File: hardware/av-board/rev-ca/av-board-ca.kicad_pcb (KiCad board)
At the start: 4 copper layers, 130 x 100 mm, 284 parts, among them J1 RCA Y, J11 XIAO 5V..D7, J12 XIAO D0..D6, J13 OPTICAL, J14 RCA S/PDIF, J15 USB-C 5V, J16 JTAG, J2 RCA Pb, J20 DF40HC(3.0)-80DS, J21 DF40HC(3.0)-100DS, J22 DF40HC(3.0)-100DS, J3 RCA Pr, J4 RCA L, J5 RCA R, J6 HDMI-001, J7 SYNC, J8 VGA, Q1 2N7002, Q2 2N7002, Q3 2N7002, Q4 2N7002, SW1 TS-1187A-B-A-B, SW2 TS-1187A-B-A-B, SW3 TS-1187A-B-A-B, U1 ADV7181DBCPZ-RL, U10 TPD4E05U06DQAR, U12 TPS7A2045PDBVR, U13 SN74LVC1GU04DBVR, U14 SN74LVC1G04DBVR, U15 SN74LVC1G04DBVR, U17 MS5351M, U19 TPD4E05U06DQAR, U2 ADV7511KSTZ, U20 TPD4E05U06DQAR, U21 SN74LVC2G17DBVR, U22 SN74LVC8T245PWR, U23 SN74AVC4T245PWR, U24 ME6211C30M5G-N, U3 PCM1808PWR, U4 TLV62569DBVR, U5 TPS7A7001DDAR, U6 TPS7A7001DDAR, U7 TPS7A7001DDAR, U8 TPD4E05U06DQAR, U9 TPD4E05U06DQAR, Y1 28.63636MHz 20pF, Y2 25MHz 10pF

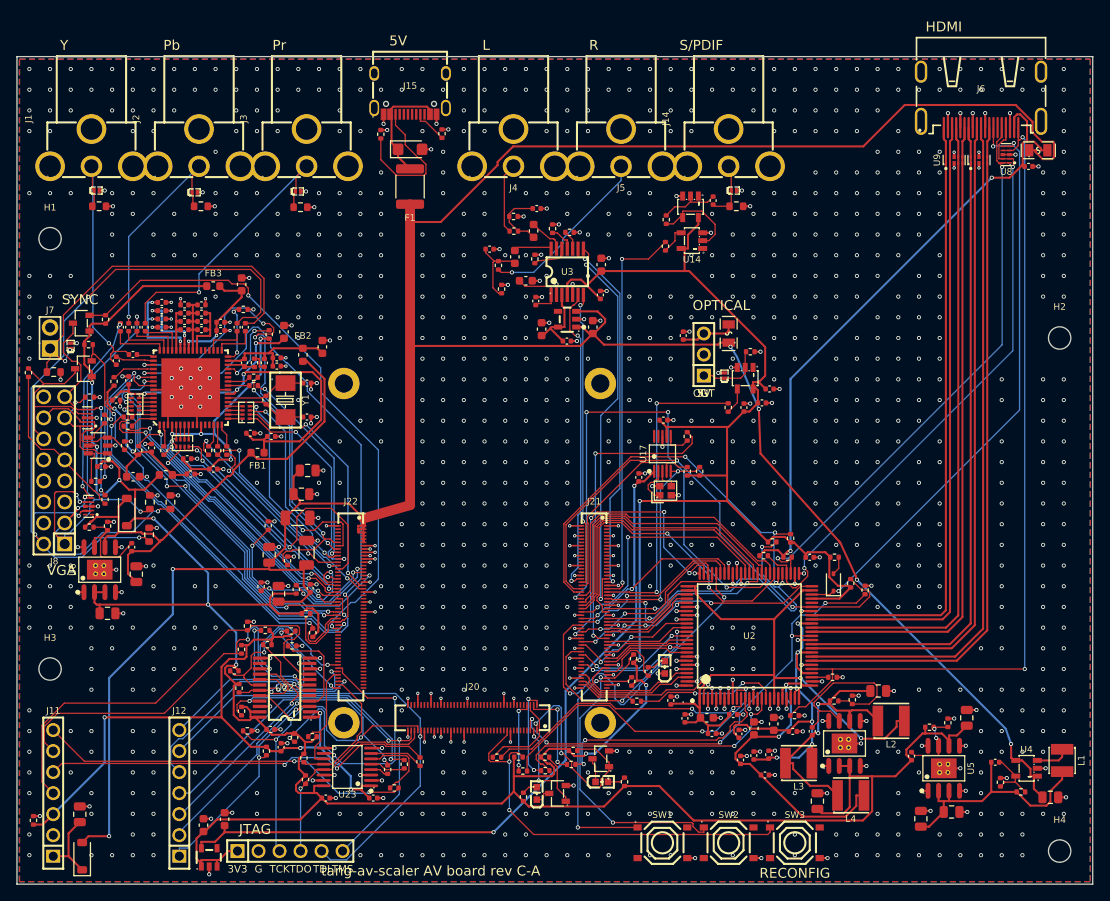
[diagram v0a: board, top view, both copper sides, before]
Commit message: AV boards: the last complete, valid design of each revision; decoupling at the pins
Each revision's board, schematic, fab files and renders are its last complete
route: DRC clean, no unconnected items, ERC clean, the board equal to its
schematic part for part (pads, values, footprints; only the mounting holes
H1-H4 have no symbol).

- Rev A: the silkscreen pass (labels clear of pads, texts and part bodies);
  copper unchanged.
- Rev B: the previous route with the silkscreen pass. Its schematic stays the
  one it was routed from: board.py now numbers eight capacitors the other way
  round, and its placement fixes (below) are not routed yet, the routes on the
  new placement having left 1 and 3 connections (review.md, Status).
- C-A: routed again on the fixed placement (try-ca-p1), the copper the router
  laid twice over taken up (218 segments).
- C-B: S/PDIF on rev B's 5-pin header instead of the coax jack, the HDMI
  receptacle next to the RCAs, the board 100 x 100 mm; routed again on the
  fixed placement (try-cb-p3). 5.4 mm of copper laid side by side in five
  nets is left (rev-c/review.md).

The review found decoupling not at the pins on every board (ADV7511 9-25 mm,
DP159 6-13 mm, the bucks' input capacitor by EN, the LDOs' capacitors, the
clock LDOs 73-80 mm from their chip) and C's VBUS_IN 0.25 mm wide for 2 A:
- parts.py: Part.at = "REF.PAD", the one pad a capacitor or filter serves;
  circuits, carrier.py and board.py name it for every regulator and supply pin
- pcbkit.py placer: ESD parts first, then small chips, then the at= capacitors
  and bias parts in board.py order; mean pin-to-capacitor distance on the
  placements: rev B 8.1 -> 3.6 mm, C-A 6.3 -> 3.3, C-B 5.5 -> 3.4
- rev C: VBUS_IN 0.7/1.2 mm into the TVS and fuse; rev B and C: the coax
  slicer placed first (SPDIF_AC a bias net); rev B: the buck U4 turned over

Kit: the silkscreen pass (labels clear of pads, texts, parts and the SOM,
reserved in the placer); prune takes up copper lying on another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
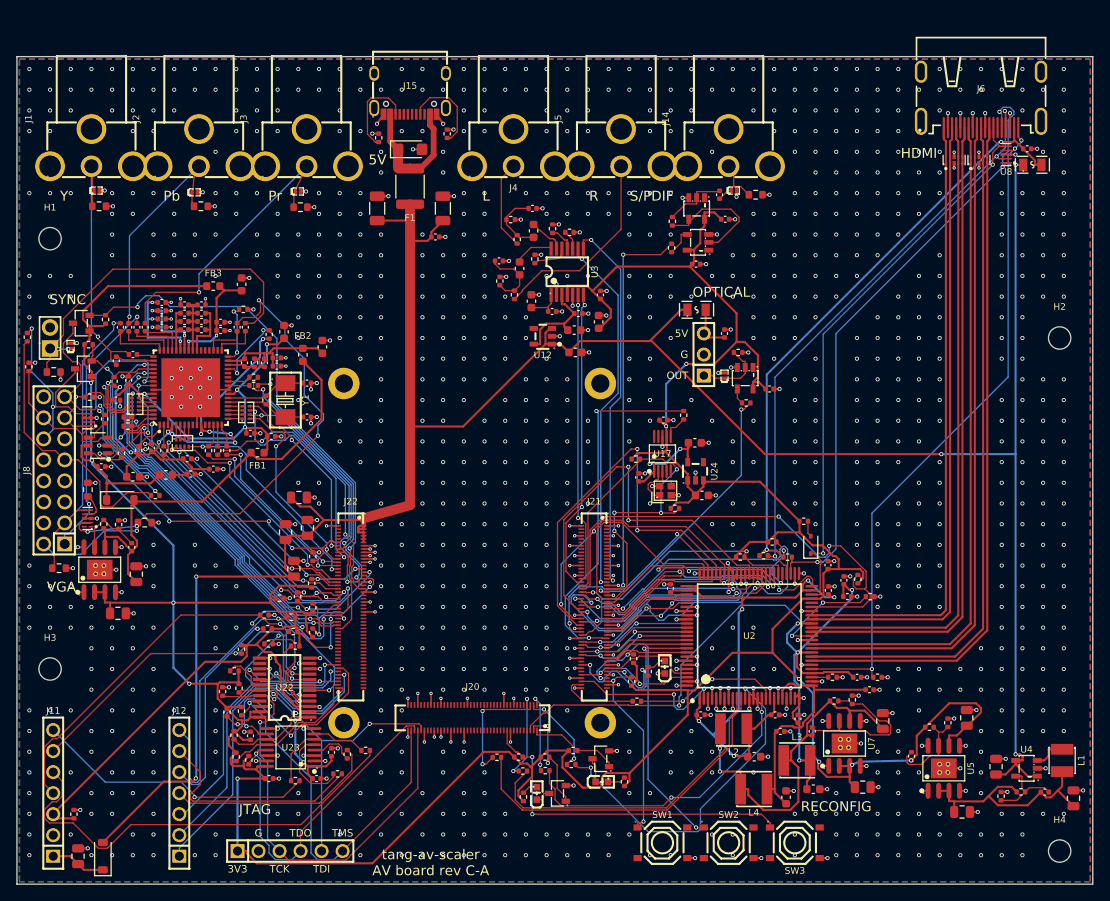
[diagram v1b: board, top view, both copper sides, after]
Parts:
- C11, C14, C8: value 10u -> 220p; footprint Capacitor_SMD:C_0805_2012Metric -> Capacitor_SMD:C_0402_1005Metric
- C12, C15, C9: value 220p -> 10u; footprint Capacitor_SMD:C_0402_1005Metric -> Capacitor_SMD:C_0805_2012Metric
- C5: value 10u -> 6.8p; footprint Capacitor_SMD:C_0805_2012Metric -> Capacitor_SMD:C_0402_1005Metric
- C6: value 6.8p -> 10u; footprint Capacitor_SMD:C_0402_1005Metric -> Capacitor_SMD:C_0805_2012Metric
- moved U24 75.0 mm to (182.0, 100.1)
- moved C80 72.8 mm to (181.9, 96.7), turned to 0 degrees
- moved C79 72.2 mm to (182.8, 103.0), turned to 0 degrees
- moved C3 45.1 mm to (150.6, 71.8), turned to 0 degrees
- moved C1 44.8 mm to (151.5, 68.3)
- moved C2 38.6 mm to (143.5, 68.3), turned to 90 degrees
- moved C93 23.8 mm to (199.9, 113.3)
- moved C70 21.2 mm to (185.6, 69.7)
- moved C92 21.1 mm to (200.3, 115.2), turned to 0 degrees
- moved L2 19.0 mm to (186.6, 131.2)
- moved C88 18.9 mm to (198.1, 114.5), turned to 90 degrees
- moved C71 18.6 mm to (182.1, 75.1)
- moved C89 18.3 mm to (179.0, 114.3), turned to 90 degrees
- moved C95 16.3 mm to (203.0, 126.5)
- moved R34 15.6 mm to (105.1, 111.8), turned to 0 degrees
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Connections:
- C11 pad 2: GND -> FB_1V8A
- C12 pad 2: FB_1V8A -> GND
- C14 pad 2: GND -> FB_1V8B
- C15 pad 2: FB_1V8B -> GND
- C5 pad 2: GND -> FB_3V6
- C6 pad 2: FB_3V6 -> GND
- C8 pad 2: GND -> FB_3V3
- C9 pad 2: FB_3V3 -> GND
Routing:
- net 3V0: track 89.6 -> 11.8 mm
- net +5V: track 344.9 -> 301.9 mm, vias 6 -> 5
- net OUT_R5: track 63.8 -> 28.0 mm, vias 4 -> 2
- net OUT_SDA: track 51.8 -> 29.0 mm, vias 3 -> 2
- net OUT_R3: track 21.1 -> 42.9 mm
- net IN_SDA: track 69.8 -> 48.2 mm
- net HDMI_HPD: track 103.2 -> 83.0 mm, vias 2 -> 3
- net XIAO_D6: track 25.3 -> 45.3 mm
- net JTAG_TDO: track 25.5 -> 42.4 mm
- net XIAO_D0: track 27.0 -> 43.7 mm, vias 2 -> 1
- net VGA_G: track 90.6 -> 75.1 mm, vias 4 -> 5
- net VGA_R: track 52.1 -> 37.4 mm, vias 4 -> 2
- net OUT_R7: track 39.1 -> 24.7 mm
- net FPGA_READY: track 25.2 -> 11.1 mm, vias 2 -> 0
- net TX_I2S0: track 27.5 -> 41.5 mm
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
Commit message: AV boards: silkscreen to JLCPCB's limits; the XIAO's way in printed on rev C
JLCPCB's silkscreen limits (its capabilities page): lines and strokes 0.15 mm
at least, text 1 mm high with a 1:6 stroke, 0.15 mm from pads.

- kit/pcbkit.py: designators and pin labels 1 mm (were 0.8 and 0.9 mm), every
  text's stroke 1:6 of its height; designators clear of the other parts'
  bodies, tried at 40 places beside their part before its own body.
  silk_tidy(): the parts' own silkscreen widened to 0.15 mm and cut back where
  it came within 0.15 mm of a pad, past the board's edge, under a text or onto
  another part's (the bigger parts first); EasyEDA's 0.12 mm pin 1 dots (too
  small to print) taken out, small marks moved clear. A second run changes
  nothing.
- Rev B, C-A, C-B: the silkscreen pass run again (--silk): only the silkscreen
  Gerbers changed. DRC: no silkscreen warnings (were 56, 63, 54); designators
  shown 36, 51, 45 (were 35, 41, 33). The trimmed footprints now differ from
  the library (DRC's lib_footprint_mismatch, noted in the reviews).
- Rev B: "XIAO, USB >" by J12 (by J11 no place was clear: it lay over copper).
- Rev C: the XIAO's way in printed beside J12, "XIAO, USB >" reading down to
  its USB-C's end (that of D0 and 5V, the sockets' pin 1, at the bottom edge);
  kit SILK_NEAR entries may carry an angle (the label beside the part).

Co-Authored-By: Claude Opus 5.5 <noreply@anthropic.com>
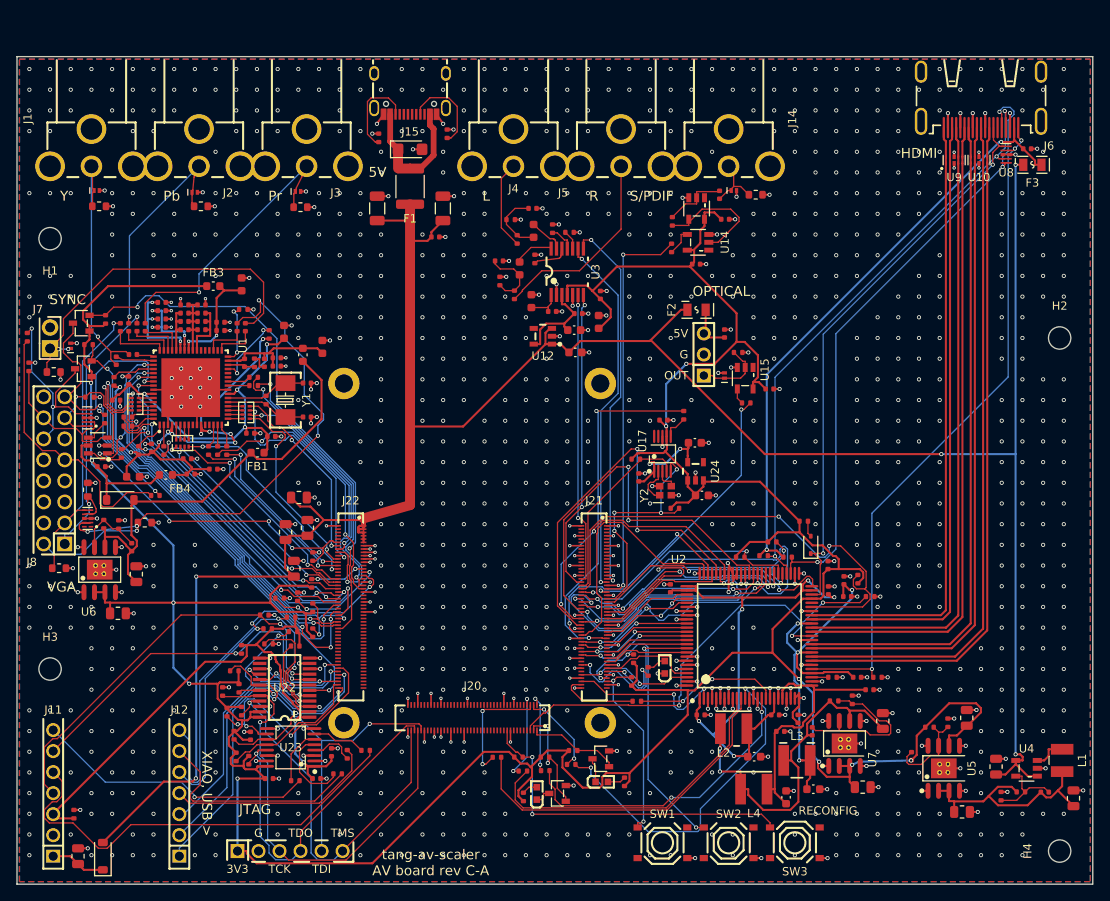
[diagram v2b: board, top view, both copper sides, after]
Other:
- board text added: "XIAO, USB >"

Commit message: AV board C-A: the TMDS pairs 5 W apart up their run, kept clear; re-routed
C-A had C-B's old faults (kit/hdmi_audit.py rev-ca, TI SPRAAR7): the pairs 3 W apart for all of
their 75-84 mm, a +5V via 0.18 mm from TMDS_D2_P (its antipad 0.03 mm from the line in In1), the
HPD via 0.62 mm from TMDS_CK, the ground pour within 0.3 mm of every pair, nothing voided under
the ESD arrays. Now (rev-ca/gen_pcb.py):
- TMDS_SPREAD 0.52: the pairs 1.27 mm (5 W) apart up their 55 mm run, as C-B's.
- TMDS_KEEP_OUT: the kit's keep-outs along the first leg too (15-17 mm from the ADV7511 to the
  corner), past the chip's break-out, round the corners and up the run; In1 and In2 voided
  under the arrays' TMDS pads.
- The first leg keeps the chip's pin pitch (3 W for about 10 mm past the break-out): spread
  there, the outer pairs would cross the HPD and OUT_INT lines that leave pins 30 and 45 beside
  CK and D2.

Re-routed (h10, the best of 12 on the Spark): DRC 0 errors, 0 unconnected; schematic = board.py
(1063 pins); the generator's placement, copper and keep-outs reproduced on the routed board (to
the router's 0.1 um rounding; three fanout vias the router made needless pruned). Lines 74.4-84.4
mm, 5 ps within a pair, 58 ps between pairs. Analog lines: nothing digital within 0.5 mm but the
crystal pin beside LLC every route has, an LLC via 0.32 mm from XTAL1 and the PLL supply 0.499 mm
from IN_C1 (KiCad's DRC with the rule, vias counted); RCA_SYNC no longer has the vias by the
DDC clock. The pixel bus spreads further: 10.3-73.3 mm (about 0.4 ns in 6.7 ns, R0 and R1 the
long ones), within what the FPGA's output delays trim. Left: the first leg's 3 W, and a +5V via's
antipad 0.15 mm from TMDS_CK where the pairs close up into the arrays (their break-out).

Kit: stitch() tests a via's whole disc against the via keep-outs (KiCad's polygon distance);
sampling its middle and four points round it let a TMDS strip's corner in between, and three of
the twelve routes had a ground via 0.12 mm over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
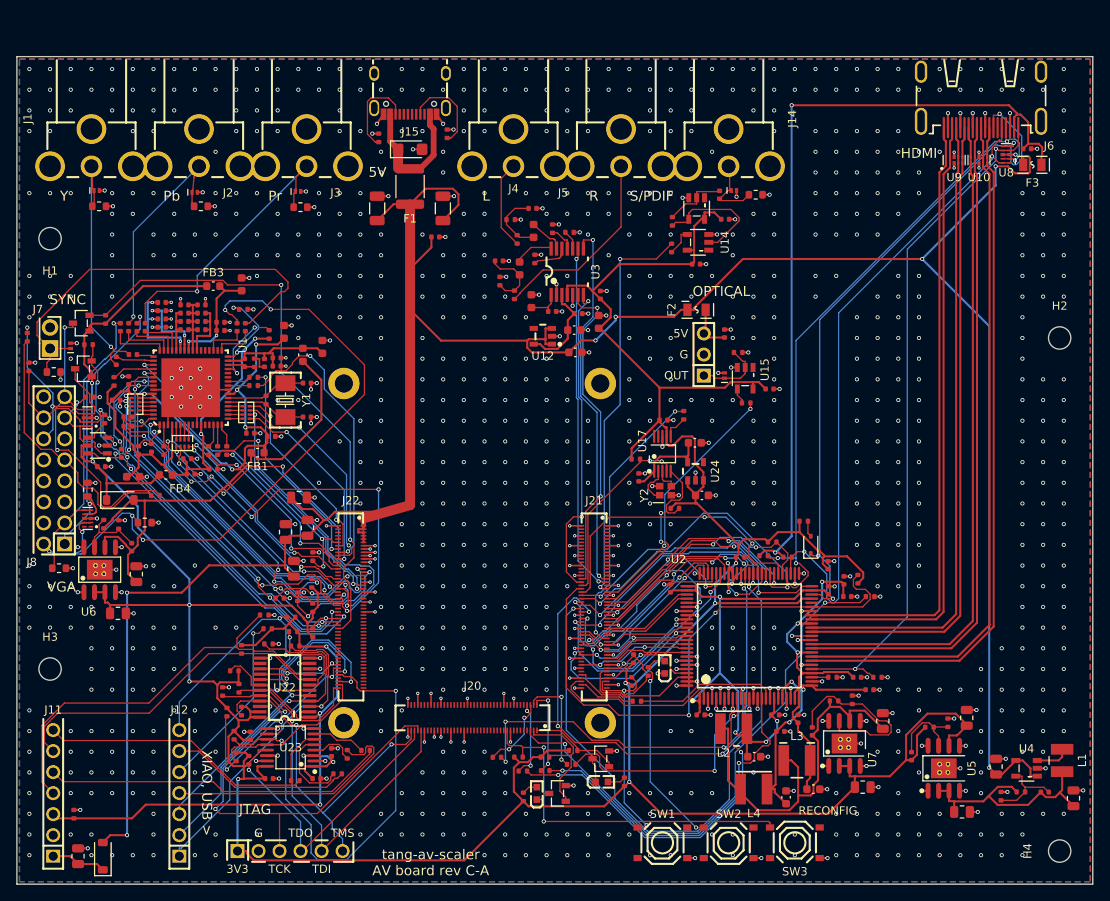
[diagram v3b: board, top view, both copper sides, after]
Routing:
- net OUT_R0: track 25.5 -> 64.4 mm, vias 2 -> 4
- net ESP_RX: track 19.5 -> 57.0 mm
- net OUT_R1: track 46.7 -> 73.3 mm
- net OUT_G5: track 49.3 -> 23.5 mm
- net HDMI_5V: track 72.7 -> 97.1 mm
- net IN_DE: track 37.3 -> 57.9 mm, vias 2 -> 6
- net OUT_R3: track 42.9 -> 22.7 mm
- net IN_HS: track 30.3 -> 47.7 mm, vias 2 -> 4
- net XIAO_D4: track 45.2 -> 28.7 mm, vias 3 -> 2
- net HDMI_CEC: track 69.6 -> 85.0 mm, vias 2 -> 4
- net +5V: track 301.9 -> 316.2 mm, vias 5 -> 7
- net IN_RESET_N: track 52.9 -> 39.6 mm, vias 6 -> 3
- net OUT_PD: track 56.6 -> 69.4 mm
- net IN_Y5: track 53.9 -> 41.5 mm
- net TX_I2S0: track 41.5 -> 29.3 mm
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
